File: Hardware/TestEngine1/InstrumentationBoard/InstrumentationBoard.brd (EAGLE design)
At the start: 100 x 80 mm, 43 parts, among them IC1 MAX31855, J1 1X2-3.5MM

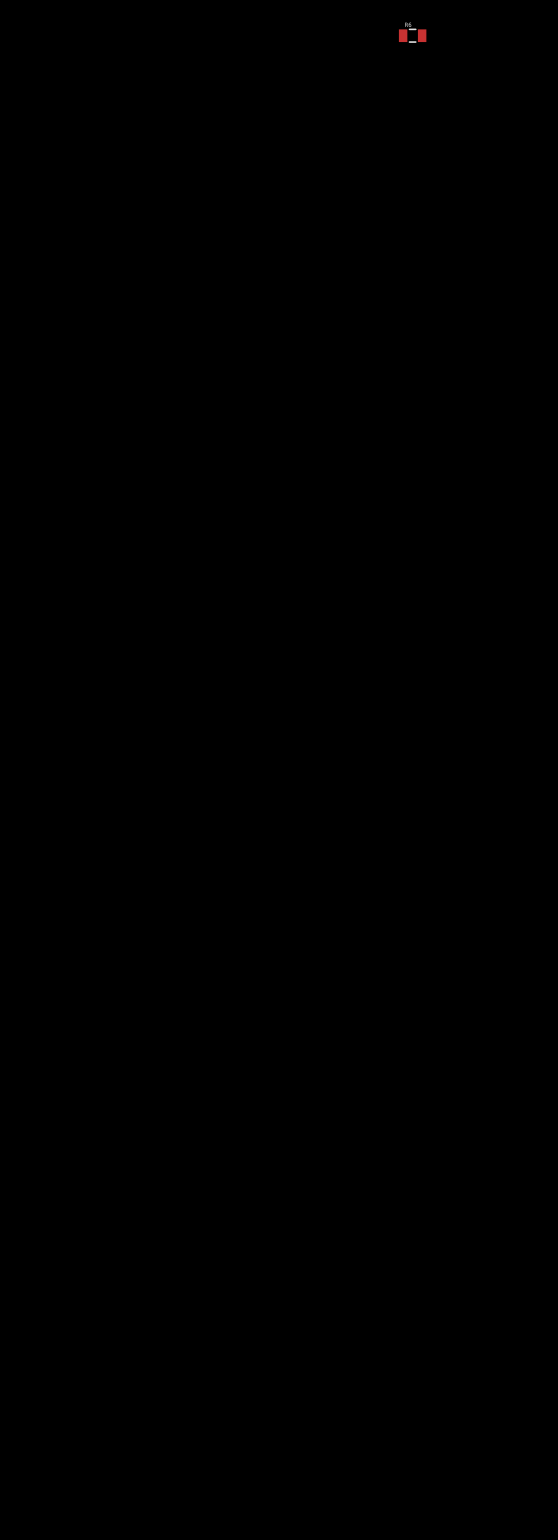
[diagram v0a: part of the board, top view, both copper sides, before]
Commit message: added user interface and saftey interlocks.
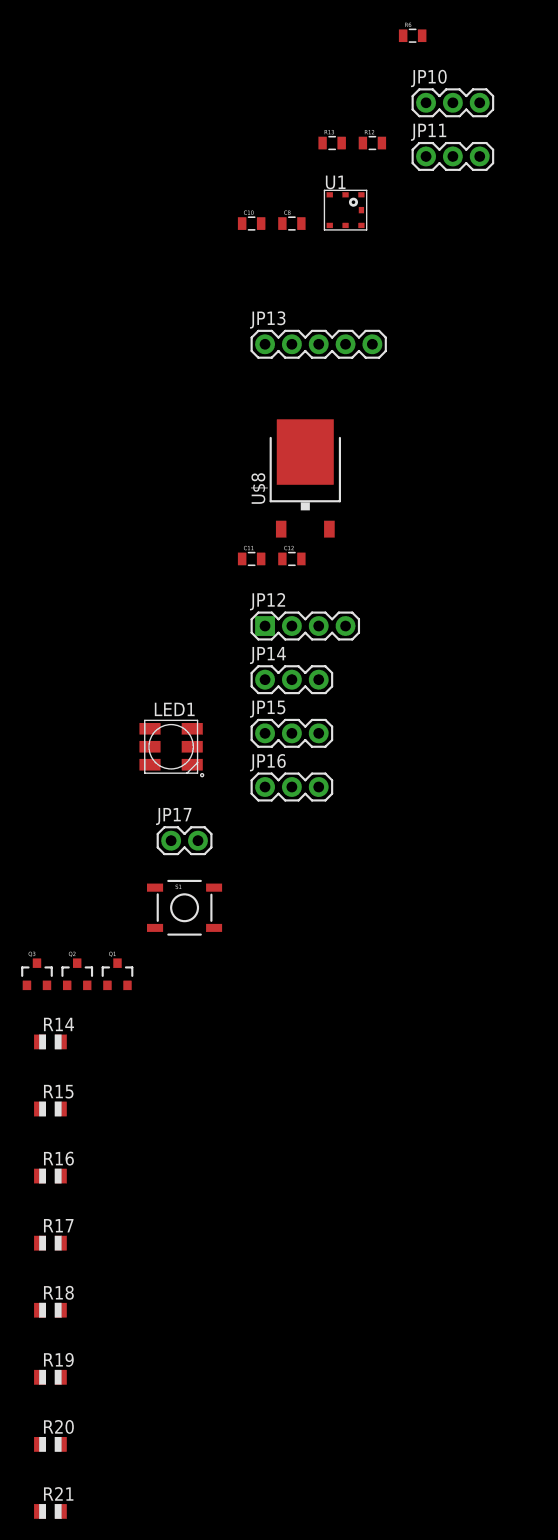
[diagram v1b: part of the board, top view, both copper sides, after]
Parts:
- added C10, C12, C8: 0.1uF, SparkFun-Capacitors:0805
- added C11: 0.33uF, SparkFun-Capacitors:0805
- added JP10, JP11, JP14, JP15, JP16: (no value), SparkFun-Connectors:1X03
- added JP12: (no value), SparkFun-Connectors:1X04
- added JP13: (no value), SparkFun-Connectors:1X05
- added JP17: M02PTH, SparkFun-Connectors:1X02
- added LED1: RGBLED5050, adafruit:RGBLED5050
- added Q1, Q2, Q3: MOSFET-NCHANNELBSS123LT1G, SparkFun-DiscreteSemi:SOT23-3
- added R12: 33, SparkFun-Resistors:0805
- added R13: 66, SparkFun-Resistors:0805
- added R14: 68, adafruit:R0805
- added R15, R16: 0, adafruit:R0805
- added R17, R18, R19, R20, R21: 10K, adafruit:R0805
- added S1: SWITCH-MOMENTARY-2SMD, SparkFun-Electromechanical:TACTILE-SWITCH-SMD
- added U$8: MC33269DTRK, RitLaunchInitiative:TO-252
- added U1: BMP180, SparkFun-Sensors:BMP180
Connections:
- net THERMOCOUPLE renamed LOADCELL
- removed net DO: IC1.7
- new net BLUE: Q1.1, R17.1
- new net GREEN: Q2.1, R18.1
- new net MISO: IC1.7, JP13.5
- new net MOSI: JP13.4
- new net N$10: LED1.1, R15.2
- new net N$15: LED1.3, R16.2
- new net N$2: JP10.2, R12.2
- new net N$3: LED1.5, Q3.3
- new net N$7: LED1.6, Q2.3
- new net N$8: LED1.4, Q1.3
- new net N$9: LED1.2, R14.2
- new net PSI_1: R12.1, R13.2
- new net PSI_2_CS: JP13.2
- new net PWM_1: JP14.1
- new net PWM_2: JP15.1
- new net PWM_3: JP16.1
- new net RED: Q3.1, R19.1
- new net SCL: JP11.2, U1.5
- new net SCLK: D1.C, JP13.3
- new net SDA: JP11.3, U1.6
- new net SW_1: R20.1, S1.1
- new net THERMOCOUPLE_CS: D2.C
- new net TILTSWITCH_1: JP17.1, R21.1
- net +3V3: now also C10.1, C8.1, JP12.2, JP17.2, R14.1, R15.1, R16.1, S1.3, U1.2, U1.3
- net 12V: now also C11.1, JP12.4, U$8.3
- net 5V: now also C12.1, JP10.1, JP12.3, JP14.2, JP15.2, JP16.2, U$8.2
- net CS: no longer D2.C
- net GND: now also C10.2, C8.2, JP10.3, JP11.1, JP12.1, JP13.1, JP14.3, JP15.3, JP16.3, Q1.2, Q2.2, Q3.2, R13.1, R17.2, R18.2, R19.2, R20.2, R21.2, U1.7
- net N$12: now also C11.2, C12.2, U$8.1
- net SCK: no longer D1.C

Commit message: routed alternet Pressure sense adapter board
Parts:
- R7: value 10K -> 1K
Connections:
- net N$20: now also U$1.16; no longer U$1.15
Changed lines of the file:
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@@
 <element name="C6" library="SparkFun-Capacitors" package="0805" value="1uF" x="-77.47" y="2.54"/>
 <element name="C7" library="SparkFun-Capacitors" package="0805" value="1uF" x="-81.28" y="2.54"/>
-<element name="R7" library="adafruit" package="R0805" value="10K" x="-83.82" y="-3.81"/>
+<element name="R7" library="adafruit" package="R0805" value="1K" x="-83.82" y="-3.81"/>
 <element name="JP5" library="SparkFun-Connectors" package="1X04" value="" x="-83.82" y="-10.16"/>
 <element name="U$4" library="RitLaunchInitiative" package="TO-252" value="FDD3706" x="-92.71" y="-5.08">
@@
 </signal>
 <signal name="N$20">
-<contactref element="U$1" pad="15"/>
 <contactref element="U$1" pad="4"/>
 <contactref element="JP5" pad="3"/>
+<contactref element="U$1" pad="16"/>
 <wire x1="-26.035" y1="31.69" x2="-78.74" y2="-10.16" width="0" layer="19" extent="1-1"/>
-<wire x1="-28.575" y1="36.89" x2="-26.035" y2="31.69" width="0" layer="19" extent="1-1"/>
+<wire x1="-29.845" y1="36.89" x2="-26.035" y2="31.69" width="0" layer="19" extent="1-1"/>
 </signal>
 <signal name="N$18">

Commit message: added various components
extra bulk capacitance
power leds
battery voltage measurement
added extra analog channels
Back EMF protection diodes
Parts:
- added C13, C16: 10uF, SparkFun-Capacitors:0805
- added C14, C17, C19: 0.1uf, SparkFun-Capacitors:0805
- added C15, C18: 100pF, SparkFun-Capacitors:0805
- added D3, D4, D5, D6: B340A, SparkFun-DiscreteSemi:SMA-DIODE
- added D7, D8, D9: (no value), SparkFun-LED:LED-1206
- added JP18: M02PTH, SparkFun-Connectors:1X02
- added JP19, JP20: (no value), SparkFun-Connectors:1X03
- added R22: 9k, adafruit:R0805
- added R23: 3k, adafruit:R0805
- added R24: 10k, SparkFun-Resistors:0805
- added R25: 1.7k, SparkFun-Resistors:0805
- added R26: 3.3k, SparkFun-Resistors:0805
- added R27: 100, adafruit:R0805
- added R28: 220, adafruit:R0805
- added R29: 680, adafruit:R0805
- R12: value 33 -> 1.7k
- R13: value 66 -> 3.3k
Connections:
- removed net MOSI: JP13.4
- removed net PSI_2_CS: JP13.2
- new net BATTVOLTAGE: R22.2, R23.1
- new net N$21: JP19.2, R25.2
- new net N$23: D7.A, R28.2
- new net N$24: D8.A, R27.2
- new net N$25: D9.A, R29.2
- new net PSI_2: R25.1, R26.2
- new net PWM_4: JP20.1
- new net TR5: JP18.1, R24.2
- net +3V3: now also C19.2, JP18.2, R27.1
- net 12V: now also C13.1, C14.1, C15.1, C16.1, C17.1, C18.1, JP13.5, R22.1, R29.1
- net 5V: now also JP19.1, JP20.2, R28.1
- net GND: now also C13.2, C14.2, C15.2, C16.2, C17.2, C18.2, C19.1, D3.A, D4.A, D5.A, D6.A, D7.C, D8.C, D9.C, JP13.3, JP13.4, JP19.3, JP20.3, R23.2, R24.1, R26.1; no longer JP13.1
- net MISO: no longer JP13.5
- net N$17: now also D6.C
- net N$18: now also D3.C
- net N$19: now also D4.C
- net N$22: now also D5.C
- net SCL: now also JP13.2
- net SCLK: no longer JP13.3
- net SDA: now also JP13.1
